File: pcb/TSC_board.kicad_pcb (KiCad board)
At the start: 4 copper layers, 100 x 100 mm, 134 parts, among them IC1 TS3021ILT, IC2 TS3021ILT, IC3 TS3021ILT, IC4 TS3021ILT, IC5 NL17SZ17DFT2G, IC6 NL17SZ17DFT2G, IC7 NL17SZ17DFT2G, IC8 NL17SZ17DFT2G, J1 Conn_01x05_Socket, J2 Conn_01x05_Socket, J3 Conn_01x04_Socket, J4 Conn_01x04_Socket, U1 GAQY212GS, U13 GAQY212GS, U14 GAQY212GS, U15 GAQY212GS, U16 GAQY212GS, U17 GAQY212GS, U18 GAQY212GS, U19 GAQY212GS, U2 DAC7311xDCK, U21 GAQY212GS, U22 GAQY212GS, U23 GAQY212GS, U24 GAQY212GS, U3 LM4040DBZ-5, U4 ADuM1400xRW, U5 ADuM1300xRW, U6 TEA1-0505

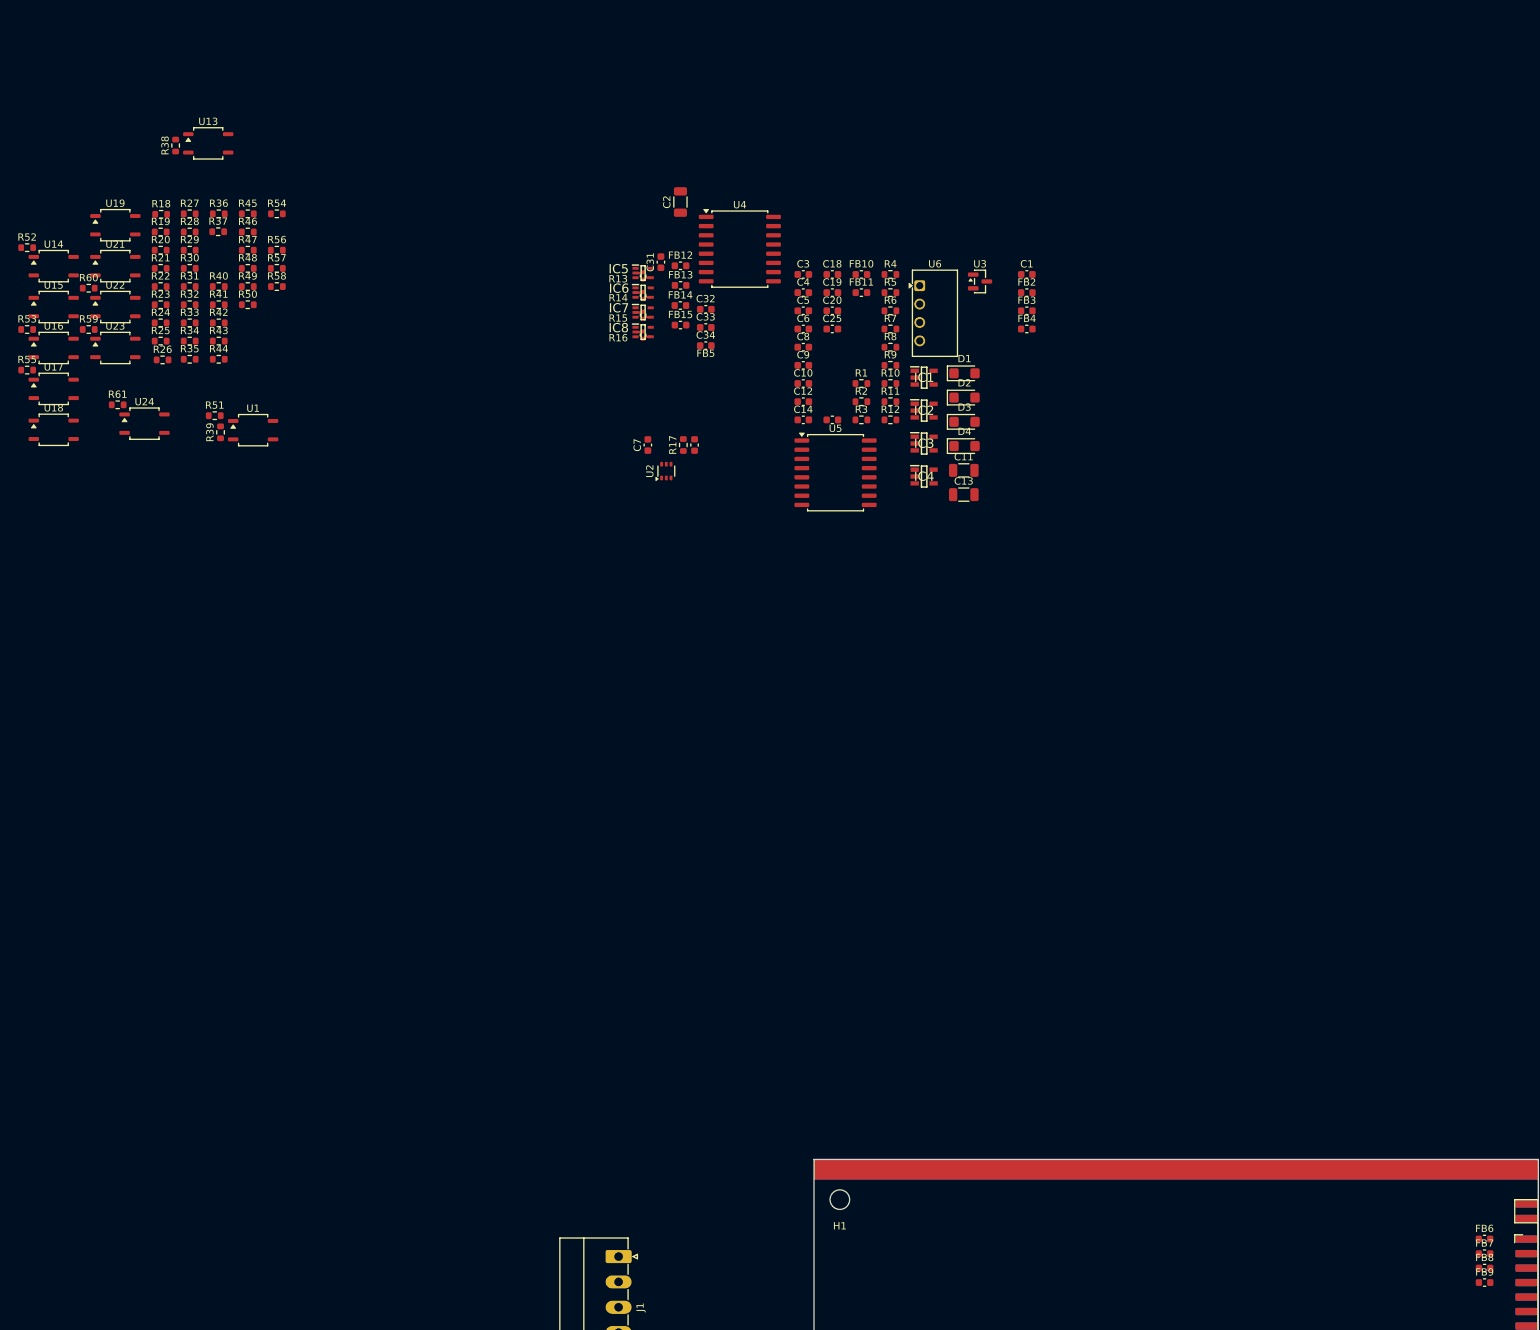
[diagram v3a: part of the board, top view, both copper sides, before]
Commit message: Remove NL17SZ17 symbol; update schematic
Delete the NL17SZ17DFT2G symbol from pcb/Frontend.kicad_sch and apply a bulk update to schematic. Many junction coordinates and UUIDs were regenerated/adjusted in Frontend.kicad_sch; related KiCad files (pcb/MCU.kicad_sch, pcb/TSC_board.kicad_pcb, pcb/TSC_board.kicad_sch) were also updated. This is primarily a cleanup refresh.
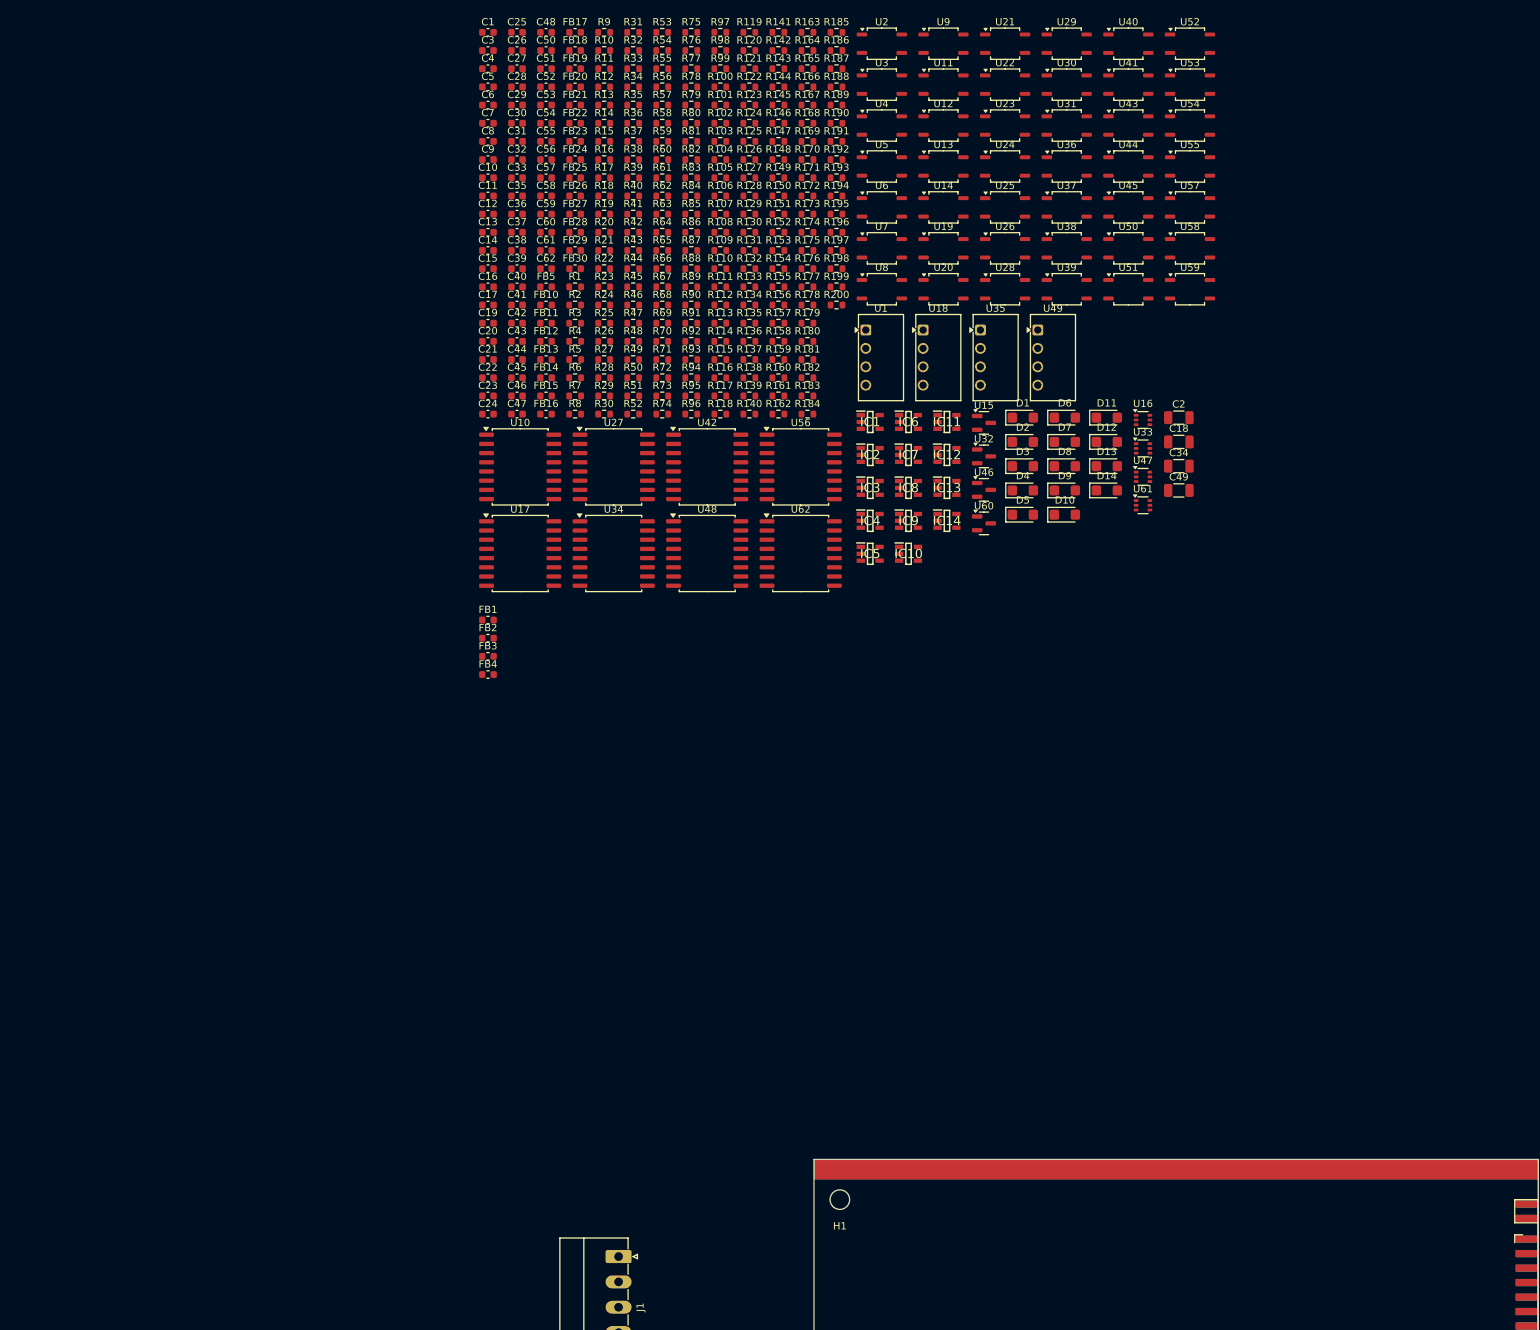
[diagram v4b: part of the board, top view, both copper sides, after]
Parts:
- removed FB6, FB7, FB8, FB9: 100R @ 100MHz, Inductor_SMD:L_0603_1608Metric
- added C15: 100n, Capacitor_SMD:C_0603_1608Metric, F.Cu at (25.0, -73.0)
- added C16: 1n, Capacitor_SMD:C_0603_1608Metric, F.Cu at (25.0, -70.5)
- added C17: 100n, Capacitor_SMD:C_0603_1608Metric, F.Cu at (25.0, -68.0)
- added C21: 100n, Capacitor_SMD:C_0603_1608Metric, F.Cu at (25.0, -60.5)
- added C22: 100n, Capacitor_SMD:C_0603_1608Metric, F.Cu at (25.0, -57.9)
- added C23: 10n, Capacitor_SMD:C_0603_1608Metric, F.Cu at (25.0, -55.4)
- added C24: 100n, Capacitor_SMD:C_0603_1608Metric, F.Cu at (25.0, -52.9)
- added C26: 100n, Capacitor_SMD:C_0603_1608Metric, F.Cu at (29.0, -103.1)
- added C27: 100n, Capacitor_SMD:C_0603_1608Metric, F.Cu at (29.0, -100.6)
- added C28: 100n, Capacitor_SMD:C_0603_1608Metric, F.Cu at (29.0, -98.1)
- added C29: 100n, Capacitor_SMD:C_0603_1608Metric, F.Cu at (29.0, -95.6)
- added C30: 10n, Capacitor_SMD:C_0603_1608Metric, F.Cu at (29.0, -93.1)
- added C35: 10n, Capacitor_SMD:C_0603_1608Metric, F.Cu at (29.0, -83.0)
- added C36: 100n, Capacitor_SMD:C_0603_1608Metric, F.Cu at (29.0, -80.5)
- added C37: 100n, Capacitor_SMD:C_0603_1608Metric, F.Cu at (29.0, -78.0)
- added C38: 100n, Capacitor_SMD:C_0603_1608Metric, F.Cu at (29.0, -75.5)
- added C39: 10n, Capacitor_SMD:C_0603_1608Metric, F.Cu at (29.0, -73.0)
- added C40: 100n, Capacitor_SMD:C_0603_1608Metric, F.Cu at (29.0, -70.5)
- added C41: 100n, Capacitor_SMD:C_0603_1608Metric, F.Cu at (29.0, -68.0)
- added C42: 100n, Capacitor_SMD:C_0603_1608Metric, F.Cu at (29.0, -65.5)
- added C43: 100n, Capacitor_SMD:C_0603_1608Metric, F.Cu at (29.0, -63.0)
- added C44: 100n, Capacitor_SMD:C_0603_1608Metric, F.Cu at (29.0, -60.5)
- added C45: 10n, Capacitor_SMD:C_0603_1608Metric, F.Cu at (29.0, -57.9)
- added C46: 100n, Capacitor_SMD:C_0603_1608Metric, F.Cu at (29.0, -55.4)
- added C47: 1n, Capacitor_SMD:C_0603_1608Metric, F.Cu at (29.0, -52.9)
- added C48: 100n, Capacitor_SMD:C_0603_1608Metric, F.Cu at (33.0, -105.6)
- added C49: 10u, Capacitor_SMD:C_1206_3216Metric, F.Cu at (120.4, -42.4)
- added C50: 10n, Capacitor_SMD:C_0603_1608Metric, F.Cu at (33.0, -103.1)
- added C51: 100n, Capacitor_SMD:C_0603_1608Metric, F.Cu at (33.0, -100.6)
- added C52: 100n, Capacitor_SMD:C_0603_1608Metric, F.Cu at (33.0, -98.1)
- added C53: 100n, Capacitor_SMD:C_0603_1608Metric, F.Cu at (33.0, -95.6)
- added C54: 10n, Capacitor_SMD:C_0603_1608Metric, F.Cu at (33.0, -93.1)
- added C55: 100n, Capacitor_SMD:C_0603_1608Metric, F.Cu at (33.0, -90.6)
- added C56: 100n, Capacitor_SMD:C_0603_1608Metric, F.Cu at (33.0, -88.1)
- added C57: 100n, Capacitor_SMD:C_0603_1608Metric, F.Cu at (33.0, -85.5)
- added C58: 100n, Capacitor_SMD:C_0603_1608Metric, F.Cu at (33.0, -83.0)
- added C59: 100n, Capacitor_SMD:C_0603_1608Metric, F.Cu at (33.0, -80.5)
- added C60: 10n, Capacitor_SMD:C_0603_1608Metric, F.Cu at (33.0, -78.0)
- added C61: 100n, Capacitor_SMD:C_0603_1608Metric, F.Cu at (33.0, -75.5)
- added C62: 1n, Capacitor_SMD:C_0603_1608Metric, F.Cu at (33.0, -73.0)
- added D10: SMF5.0CA, Diode_SMD:D_SMF, F.Cu at (104.7, -39.0)
- added D11: SMF5.0CA, Diode_SMD:D_SMF, F.Cu at (110.5, -52.4)
- added D12: SMF5.0CA, Diode_SMD:D_SMF, F.Cu at (110.5, -49.1)
- added D13: SMF5.0CA, Diode_SMD:D_SMF, F.Cu at (110.5, -45.7)
- added D14: SMF5.0CA, Diode_SMD:D_SMF, F.Cu at (110.5, -42.4)
- added D5: SMF5.0CA, Diode_SMD:D_SMF, F.Cu at (98.9, -39.0)
- added D6: SMF5.0CA, Diode_SMD:D_SMF, F.Cu at (104.7, -52.4)
- added D7: SMF5.0CA, Diode_SMD:D_SMF, F.Cu at (104.7, -49.1)
- added D8: SMF5.0CA, Diode_SMD:D_SMF, F.Cu at (104.7, -45.7)
- added D9: SMF5.0CA, Diode_SMD:D_SMF, F.Cu at (104.7, -42.4)
- added FB16: 100R @ 100MHz, Inductor_SMD:L_0603_1608Metric, F.Cu at (33.0, -52.9)
- added FB17: 100R @ 100MHz, Inductor_SMD:L_0603_1608Metric, F.Cu at (37.1, -105.6)
- added FB18: 100R @ 100MHz, Inductor_SMD:L_0603_1608Metric, F.Cu at (37.1, -103.1)
- added FB19: 100R @ 100MHz, Inductor_SMD:L_0603_1608Metric, F.Cu at (37.1, -100.6)
- added FB20: 100R @ 100MHz, Inductor_SMD:L_0603_1608Metric, F.Cu at (37.1, -98.1)
- added FB21: 100R @ 100MHz, Inductor_SMD:L_0603_1608Metric, F.Cu at (37.1, -95.6)
- added FB22: 100R @ 100MHz, Inductor_SMD:L_0603_1608Metric, F.Cu at (37.1, -93.1)
- added FB23: 100R @ 100MHz, Inductor_SMD:L_0603_1608Metric, F.Cu at (37.1, -90.6)
- added FB24: 100R @ 100MHz, Inductor_SMD:L_0603_1608Metric, F.Cu at (37.1, -88.1)
- added FB25: 100R @ 100MHz, Inductor_SMD:L_0603_1608Metric, F.Cu at (37.1, -85.5)
- added FB26: 100R @ 100MHz, Inductor_SMD:L_0603_1608Metric, F.Cu at (37.1, -83.0)
- added FB27: 100R @ 100MHz, Inductor_SMD:L_0603_1608Metric, F.Cu at (37.1, -80.5)
- added FB28: 100R @ 100MHz, Inductor_SMD:L_0603_1608Metric, F.Cu at (37.1, -78.0)
- added FB29: 100R @ 100MHz, Inductor_SMD:L_0603_1608Metric, F.Cu at (37.1, -75.5)
- added FB30: 100R @ 100MHz, Inductor_SMD:L_0603_1608Metric, F.Cu at (37.1, -73.0)
- added IC10: TS3021ILT, TS3021ILT:SOT95P280X145-5N, F.Cu at (83.1, -33.6)
- added IC11: TS3021ILT, TS3021ILT:SOT95P280X145-5N, F.Cu at (88.4, -51.8)
- added IC12: TS3021ILT, TS3021ILT:SOT95P280X145-5N, F.Cu at (88.4, -47.3)
- added IC13: TS3021ILT, TS3021ILT:SOT95P280X145-5N, F.Cu at (88.4, -42.7)
- added IC14: TS3021ILT, TS3021ILT:SOT95P280X145-5N, F.Cu at (88.4, -38.2)
- added IC9: TS3021ILT, TS3021ILT:SOT95P280X145-5N, F.Cu at (83.1, -38.2)
- added R100: 10k, Resistor_SMD:R_0603_1608Metric, F.Cu at (57.1, -98.1)
- added R101: 10k, Resistor_SMD:R_0603_1608Metric, F.Cu at (57.1, -95.6)
- added R102: 100, Resistor_SMD:R_0603_1608Metric, F.Cu at (57.1, -93.1)
- added R103: 10k, Resistor_SMD:R_0603_1608Metric, F.Cu at (57.1, -90.6)
- added R104: 10k, Resistor_SMD:R_0603_1608Metric, F.Cu at (57.1, -88.1)
- added R105: 10k, Resistor_SMD:R_0603_1608Metric, F.Cu at (57.1, -85.5)
- added R106: 10k, Resistor_SMD:R_0603_1608Metric, F.Cu at (57.1, -83.0)
- added R107: 50k, Resistor_SMD:R_0603_1608Metric, F.Cu at (57.1, -80.5)
- added R108: 1k, Resistor_SMD:R_0603_1608Metric, F.Cu at (57.1, -78.0)
- added R109: 100, Resistor_SMD:R_0603_1608Metric, F.Cu at (57.1, -75.5)
- added R110: 10k, Resistor_SMD:R_0603_1608Metric, F.Cu at (57.1, -73.0)
- added R111: 10k, Resistor_SMD:R_0603_1608Metric, F.Cu at (57.1, -70.5)
- added R112: 10k, Resistor_SMD:R_0603_1608Metric, F.Cu at (57.1, -68.0)
- added R113: 10k, Resistor_SMD:R_0603_1608Metric, F.Cu at (57.1, -65.5)
- added R114: 330R, Resistor_SMD:R_0603_1608Metric, F.Cu at (57.1, -63.0)
- added R115: 50k, Resistor_SMD:R_0603_1608Metric, F.Cu at (57.1, -60.5)
- added R116: 1k, Resistor_SMD:R_0603_1608Metric, F.Cu at (57.1, -57.9)
- added R117: 100, Resistor_SMD:R_0603_1608Metric, F.Cu at (57.1, -55.4)
- added R118: 470, Resistor_SMD:R_0603_1608Metric, F.Cu at (57.1, -52.9)
- added R119: 470, Resistor_SMD:R_0603_1608Metric, F.Cu at (61.1, -105.6)
- added R120: 470, Resistor_SMD:R_0603_1608Metric, F.Cu at (61.1, -103.1)
- added R121: 10k, Resistor_SMD:R_0603_1608Metric, F.Cu at (61.1, -100.6)
- added R122: 10k, Resistor_SMD:R_0603_1608Metric, F.Cu at (61.1, -98.1)
- added R123: 10k, Resistor_SMD:R_0603_1608Metric, F.Cu at (61.1, -95.6)
- added R124: 50k, Resistor_SMD:R_0603_1608Metric, F.Cu at (61.1, -93.1)
- added R125: 10k, Resistor_SMD:R_0603_1608Metric, F.Cu at (61.1, -90.6)
- added R126: 10k, Resistor_SMD:R_0603_1608Metric, F.Cu at (61.1, -88.1)
- added R127: 10k, Resistor_SMD:R_0603_1608Metric, F.Cu at (61.1, -85.5)
- added R128: 1k, Resistor_SMD:R_0603_1608Metric, F.Cu at (61.1, -83.0)
- added R129: 100, Resistor_SMD:R_0603_1608Metric, F.Cu at (61.1, -80.5)
- added R130: 470, Resistor_SMD:R_0603_1608Metric, F.Cu at (61.1, -78.0)
- added R131: 470, Resistor_SMD:R_0603_1608Metric, F.Cu at (61.1, -75.5)
- added R132: 470, Resistor_SMD:R_0603_1608Metric, F.Cu at (61.1, -73.0)
- added R133: 10k, Resistor_SMD:R_0603_1608Metric, F.Cu at (61.1, -70.5)
- added R134: 10k, Resistor_SMD:R_0603_1608Metric, F.Cu at (61.1, -68.0)
- added R135: 10k, Resistor_SMD:R_0603_1608Metric, F.Cu at (61.1, -65.5)
- added R136: 10k, Resistor_SMD:R_0603_1608Metric, F.Cu at (61.1, -63.0)
- added R137: 10k, Resistor_SMD:R_0603_1608Metric, F.Cu at (61.1, -60.5)
- added R138: 10k, Resistor_SMD:R_0603_1608Metric, F.Cu at (61.1, -57.9)
- added R139: 50k, Resistor_SMD:R_0603_1608Metric, F.Cu at (61.1, -55.4)
- added R140: 10k, Resistor_SMD:R_0603_1608Metric, F.Cu at (61.1, -52.9)
- added R141: 10k, Resistor_SMD:R_0603_1608Metric, F.Cu at (65.1, -105.6)
- added R142: 10k, Resistor_SMD:R_0603_1608Metric, F.Cu at (65.1, -103.1)
- added R143: 470, Resistor_SMD:R_0603_1608Metric, F.Cu at (65.1, -100.6)
- added R144: 470, Resistor_SMD:R_0603_1608Metric, F.Cu at (65.1, -98.1)
- added R145: 1k, Resistor_SMD:R_0603_1608Metric, F.Cu at (65.1, -95.6)
- added R146: 470, Resistor_SMD:R_0603_1608Metric, F.Cu at (65.1, -93.1)
- added R147: 10k, Resistor_SMD:R_0603_1608Metric, F.Cu at (65.1, -90.6)
- added R148: 10k, Resistor_SMD:R_0603_1608Metric, F.Cu at (65.1, -88.1)
- added R149: 10k, Resistor_SMD:R_0603_1608Metric, F.Cu at (65.1, -85.5)
- added R150: 100, Resistor_SMD:R_0603_1608Metric, F.Cu at (65.1, -83.0)
- added R151: 10k, Resistor_SMD:R_0603_1608Metric, F.Cu at (65.1, -80.5)
- added R152: 10k, Resistor_SMD:R_0603_1608Metric, F.Cu at (65.1, -78.0)
- added R153: 10k, Resistor_SMD:R_0603_1608Metric, F.Cu at (65.1, -75.5)
- added R154: 10k, Resistor_SMD:R_0603_1608Metric, F.Cu at (65.1, -73.0)
- added R155: 10k, Resistor_SMD:R_0603_1608Metric, F.Cu at (65.1, -70.5)
- added R156: 10k, Resistor_SMD:R_0603_1608Metric, F.Cu at (65.1, -68.0)
- added R157: 330R, Resistor_SMD:R_0603_1608Metric, F.Cu at (65.1, -65.5)
- added R158: 50k, Resistor_SMD:R_0603_1608Metric, F.Cu at (65.1, -63.0)
- added R159: 1k, Resistor_SMD:R_0603_1608Metric, F.Cu at (65.1, -60.5)
- added R160: 100, Resistor_SMD:R_0603_1608Metric, F.Cu at (65.1, -57.9)
- added R161: 470, Resistor_SMD:R_0603_1608Metric, F.Cu at (65.1, -55.4)
- added R162: 470, Resistor_SMD:R_0603_1608Metric, F.Cu at (65.1, -52.9)
- added R163: 470, Resistor_SMD:R_0603_1608Metric, F.Cu at (69.1, -105.6)
- added R164: 10k, Resistor_SMD:R_0603_1608Metric, F.Cu at (69.1, -103.1)
- added R165: 10k, Resistor_SMD:R_0603_1608Metric, F.Cu at (69.1, -100.6)
- added R166: 10k, Resistor_SMD:R_0603_1608Metric, F.Cu at (69.1, -98.1)
- added R167: 50k, Resistor_SMD:R_0603_1608Metric, F.Cu at (69.1, -95.6)
- added R168: 10k, Resistor_SMD:R_0603_1608Metric, F.Cu at (69.1, -93.1)
- added R169: 10k, Resistor_SMD:R_0603_1608Metric, F.Cu at (69.1, -90.6)
- added R170: 10k, Resistor_SMD:R_0603_1608Metric, F.Cu at (69.1, -88.1)
- added R171: 1k, Resistor_SMD:R_0603_1608Metric, F.Cu at (69.1, -85.5)
- added R172: 100, Resistor_SMD:R_0603_1608Metric, F.Cu at (69.1, -83.0)
- added R173: 470, Resistor_SMD:R_0603_1608Metric, F.Cu at (69.1, -80.5)
- added R174: 470, Resistor_SMD:R_0603_1608Metric, F.Cu at (69.1, -78.0)
- added R175: 470, Resistor_SMD:R_0603_1608Metric, F.Cu at (69.1, -75.5)
- added R176: 10k, Resistor_SMD:R_0603_1608Metric, F.Cu at (69.1, -73.0)
- added R177: 10k, Resistor_SMD:R_0603_1608Metric, F.Cu at (69.1, -70.5)
- added R178: 10k, Resistor_SMD:R_0603_1608Metric, F.Cu at (69.1, -68.0)
- added R179: 10k, Resistor_SMD:R_0603_1608Metric, F.Cu at (69.1, -65.5)
- added R180: 10k, Resistor_SMD:R_0603_1608Metric, F.Cu at (69.1, -63.0)
- added R181: 10k, Resistor_SMD:R_0603_1608Metric, F.Cu at (69.1, -60.5)
- added R182: 50k, Resistor_SMD:R_0603_1608Metric, F.Cu at (69.1, -57.9)
- added R183: 10k, Resistor_SMD:R_0603_1608Metric, F.Cu at (69.1, -55.4)
- added R184: 10k, Resistor_SMD:R_0603_1608Metric, F.Cu at (69.1, -52.9)
- added R185: 10k, Resistor_SMD:R_0603_1608Metric, F.Cu at (73.1, -105.6)
- added R186: 470, Resistor_SMD:R_0603_1608Metric, F.Cu at (73.1, -103.1)
- added R187: 470, Resistor_SMD:R_0603_1608Metric, F.Cu at (73.1, -100.6)
- added R188: 1k, Resistor_SMD:R_0603_1608Metric, F.Cu at (73.1, -98.1)
- added R189: 470, Resistor_SMD:R_0603_1608Metric, F.Cu at (73.1, -95.6)
- added R190: 10k, Resistor_SMD:R_0603_1608Metric, F.Cu at (73.1, -93.1)
- added R191: 10k, Resistor_SMD:R_0603_1608Metric, F.Cu at (73.1, -90.6)
- added R192: 10k, Resistor_SMD:R_0603_1608Metric, F.Cu at (73.1, -88.1)
- added R193: 100, Resistor_SMD:R_0603_1608Metric, F.Cu at (73.1, -85.5)
- added R194: 10k, Resistor_SMD:R_0603_1608Metric, F.Cu at (73.1, -83.0)
- added R195: 10k, Resistor_SMD:R_0603_1608Metric, F.Cu at (73.1, -80.5)
- added R196: 10k, Resistor_SMD:R_0603_1608Metric, F.Cu at (73.1, -78.0)
- added R197: 10k, Resistor_SMD:R_0603_1608Metric, F.Cu at (73.1, -75.5)
- added R198: 10k, Resistor_SMD:R_0603_1608Metric, F.Cu at (73.1, -73.0)
- added R199: 10k, Resistor_SMD:R_0603_1608Metric, F.Cu at (73.1, -70.5)
- added R200: 330R, Resistor_SMD:R_0603_1608Metric, F.Cu at (73.1, -68.0)
- added R62: 470, Resistor_SMD:R_0603_1608Metric, F.Cu at (49.1, -83.0)
- added R63: 470, Resistor_SMD:R_0603_1608Metric, F.Cu at (49.1, -80.5)
- added R64: 470, Resistor_SMD:R_0603_1608Metric, F.Cu at (49.1, -78.0)
- added R65: 10k, Resistor_SMD:R_0603_1608Metric, F.Cu at (49.1, -75.5)
- added R66: 10k, Resistor_SMD:R_0603_1608Metric, F.Cu at (49.1, -73.0)
- added R67: 10k, Resistor_SMD:R_0603_1608Metric, F.Cu at (49.1, -70.5)
- added R68: 10k, Resistor_SMD:R_0603_1608Metric, F.Cu at (49.1, -68.0)
- added R69: 50k, Resistor_SMD:R_0603_1608Metric, F.Cu at (49.1, -65.5)
- added R70: 10k, Resistor_SMD:R_0603_1608Metric, F.Cu at (49.1, -63.0)
- added R71: 10k, Resistor_SMD:R_0603_1608Metric, F.Cu at (49.1, -60.5)
- added R72: 10k, Resistor_SMD:R_0603_1608Metric, F.Cu at (49.1, -57.9)
- added R73: 10k, Resistor_SMD:R_0603_1608Metric, F.Cu at (49.1, -55.4)
- added R74: 1k, Resistor_SMD:R_0603_1608Metric, F.Cu at (49.1, -52.9)
- added R75: 100, Resistor_SMD:R_0603_1608Metric, F.Cu at (53.1, -105.6)
- added R76: 470, Resistor_SMD:R_0603_1608Metric, F.Cu at (53.1, -103.1)
- added R77: 470, Resistor_SMD:R_0603_1608Metric, F.Cu at (53.1, -100.6)
- added R78: 470, Resistor_SMD:R_0603_1608Metric, F.Cu at (53.1, -98.1)
- added R79: 470, Resistor_SMD:R_0603_1608Metric, F.Cu at (53.1, -95.6)
- added R80: 10k, Resistor_SMD:R_0603_1608Metric, F.Cu at (53.1, -93.1)
- added R81: 10k, Resistor_SMD:R_0603_1608Metric, F.Cu at (53.1, -90.6)
- added R82: 10k, Resistor_SMD:R_0603_1608Metric, F.Cu at (53.1, -88.1)
- added R83: 10k, Resistor_SMD:R_0603_1608Metric, F.Cu at (53.1, -85.5)
- added R84: 10k, Resistor_SMD:R_0603_1608Metric, F.Cu at (53.1, -83.0)
- added R85: 10k, Resistor_SMD:R_0603_1608Metric, F.Cu at (53.1, -80.5)
- added R86: 10k, Resistor_SMD:R_0603_1608Metric, F.Cu at (53.1, -78.0)
- added R87: 10k, Resistor_SMD:R_0603_1608Metric, F.Cu at (53.1, -75.5)
- added R88: 50k, Resistor_SMD:R_0603_1608Metric, F.Cu at (53.1, -73.0)
- added R89: 10k, Resistor_SMD:R_0603_1608Metric, F.Cu at (53.1, -70.5)
- added R90: 10k, Resistor_SMD:R_0603_1608Metric, F.Cu at (53.1, -68.0)
- added R91: 10k, Resistor_SMD:R_0603_1608Metric, F.Cu at (53.1, -65.5)
- added R92: 10k, Resistor_SMD:R_0603_1608Metric, F.Cu at (53.1, -63.0)
- added R93: 470, Resistor_SMD:R_0603_1608Metric, F.Cu at (53.1, -60.5)
- added R94: 470, Resistor_SMD:R_0603_1608Metric, F.Cu at (53.1, -57.9)
- added R95: 470, Resistor_SMD:R_0603_1608Metric, F.Cu at (53.1, -55.4)
- added R96: 1k, Resistor_SMD:R_0603_1608Metric, F.Cu at (53.1, -52.9)
- added R97: 470, Resistor_SMD:R_0603_1608Metric, F.Cu at (57.1, -105.6)
- added R98: 10k, Resistor_SMD:R_0603_1608Metric, F.Cu at (57.1, -103.1)
- added R99: 10k, Resistor_SMD:R_0603_1608Metric, F.Cu at (57.1, -100.6)
- added U10: ADuM1400xRW, Package_SO:SOIC-16W_7.5x10.3mm_P1.27mm, F.Cu at (29.5, -45.6)
- added U11: GAQY212GS, Package_SO:SOP-4_3.8x4.1mm_P2.54mm, F.Cu at (87.9, -98.4)
- added U12: GAQY212GS, Package_SO:SOP-4_3.8x4.1mm_P2.54mm, F.Cu at (87.9, -92.8)
- added U20: GAQY212GS, Package_SO:SOP-4_3.8x4.1mm_P2.54mm, F.Cu at (87.9, -70.2)
- added U25: GAQY212GS, Package_SO:SOP-4_3.8x4.1mm_P2.54mm, F.Cu at (96.4, -81.5)
- added U26: GAQY212GS, Package_SO:SOP-4_3.8x4.1mm_P2.54mm, F.Cu at (96.4, -75.8)
- added U27: ADuM1400xRW, Package_SO:SOIC-16W_7.5x10.3mm_P1.27mm, F.Cu at (42.4, -45.6)
- added U28: GAQY212GS, Package_SO:SOP-4_3.8x4.1mm_P2.54mm, F.Cu at (96.4, -70.2)
- added U29: GAQY212GS, Package_SO:SOP-4_3.8x4.1mm_P2.54mm, F.Cu at (104.9, -104.1)
- added U30: GAQY212GS, Package_SO:SOP-4_3.8x4.1mm_P2.54mm, F.Cu at (104.9, -98.4)
- added U31: GAQY212GS, Package_SO:SOP-4_3.8x4.1mm_P2.54mm, F.Cu at (104.9, -92.8)
- added U32: LM4040DBZ-5, Package_TO_SOT_SMD:SOT-23, F.Cu at (93.5, -47.1)
- added U33: DAC7311xDCK, Package_TO_SOT_SMD:SOT-363_SC-70-6, F.Cu at (115.5, -48.2)
- added U34: ADuM1300xRW, Package_SO:SOIC-16W_7.5x10.3mm_P1.27mm, F.Cu at (42.4, -33.7)
- added U35: TEA1-0505, Converter_DCDC:Converter_DCDC_TRACO_TEA1-xxxx_THT, F.Cu at (93.0, -64.5)
- added U36: GAQY212GS, Package_SO:SOP-4_3.8x4.1mm_P2.54mm, F.Cu at (104.9, -87.1)
- added U37: GAQY212GS, Package_SO:SOP-4_3.8x4.1mm_P2.54mm, F.Cu at (104.9, -81.5)
- added U38: GAQY212GS, Package_SO:SOP-4_3.8x4.1mm_P2.54mm, F.Cu at (104.9, -75.8)
- added U39: GAQY212GS, Package_SO:SOP-4_3.8x4.1mm_P2.54mm, F.Cu at (104.9, -70.2)
- added U40: GAQY212GS, Package_SO:SOP-4_3.8x4.1mm_P2.54mm, F.Cu at (113.4, -104.1)
- added U41: GAQY212GS, Package_SO:SOP-4_3.8x4.1mm_P2.54mm, F.Cu at (113.4, -98.4)
- added U42: ADuM1300xRW, Package_SO:SOIC-16W_7.5x10.3mm_P1.27mm, F.Cu at (55.3, -45.6)
- added U43: GAQY212GS, Package_SO:SOP-4_3.8x4.1mm_P2.54mm, F.Cu at (113.4, -92.8)
- added U44: GAQY212GS, Package_SO:SOP-4_3.8x4.1mm_P2.54mm, F.Cu at (113.4, -87.1)
- added U45: GAQY212GS, Package_SO:SOP-4_3.8x4.1mm_P2.54mm, F.Cu at (113.4, -81.5)
- added U46: LM4040DBZ-5, Package_TO_SOT_SMD:SOT-23, F.Cu at (93.5, -42.5)
- added U47: DAC7311xDCK, Package_TO_SOT_SMD:SOT-363_SC-70-6, F.Cu at (115.5, -44.3)
- added U48: ADuM1300xRW, Package_SO:SOIC-16W_7.5x10.3mm_P1.27mm, F.Cu at (55.3, -33.7)
- added U49: TEA1-0505, Converter_DCDC:Converter_DCDC_TRACO_TEA1-xxxx_THT, F.Cu at (100.9, -64.5)
- added U50: GAQY212GS, Package_SO:SOP-4_3.8x4.1mm_P2.54mm, F.Cu at (113.4, -75.8)
- added U51: GAQY212GS, Package_SO:SOP-4_3.8x4.1mm_P2.54mm, F.Cu at (113.4, -70.2)
- added U52: GAQY212GS, Package_SO:SOP-4_3.8x4.1mm_P2.54mm, F.Cu at (122.0, -104.1)
- added U53: GAQY212GS, Package_SO:SOP-4_3.8x4.1mm_P2.54mm, F.Cu at (122.0, -98.4)
- added U54: GAQY212GS, Package_SO:SOP-4_3.8x4.1mm_P2.54mm, F.Cu at (122.0, -92.8)
- added U55: GAQY212GS, Package_SO:SOP-4_3.8x4.1mm_P2.54mm, F.Cu at (122.0, -87.1)
- added U56: ADuM1300xRW, Package_SO:SOIC-16W_7.5x10.3mm_P1.27mm, F.Cu at (68.2, -45.6)
- added U57: GAQY212GS, Package_SO:SOP-4_3.8x4.1mm_P2.54mm, F.Cu at (122.0, -81.5)
- added U58: GAQY212GS, Package_SO:SOP-4_3.8x4.1mm_P2.54mm, F.Cu at (122.0, -75.8)
- added U59: GAQY212GS, Package_SO:SOP-4_3.8x4.1mm_P2.54mm, F.Cu at (122.0, -70.2)
- added U60: LM4040DBZ-5, Package_TO_SOT_SMD:SOT-23, F.Cu at (93.5, -37.8)
- added U61: DAC7311xDCK, Package_TO_SOT_SMD:SOT-363_SC-70-6, F.Cu at (115.5, -40.3)
- added U62: ADuM1300xRW, Package_SO:SOIC-16W_7.5x10.3mm_P1.27mm, F.Cu at (68.2, -33.7)
- added U7: GAQY212GS, Package_SO:SOP-4_3.8x4.1mm_P2.54mm, F.Cu at (79.4, -75.8)
- added U8: GAQY212GS, Package_SO:SOP-4_3.8x4.1mm_P2.54mm, F.Cu at (79.4, -70.2)
- added U9: GAQY212GS, Package_SO:SOP-4_3.8x4.1mm_P2.54mm, F.Cu at (87.9, -104.1)
- C11, C13: value 10u -> 100n; footprint Capacitor_SMD:C_1206_3216Metric -> Capacitor_SMD:C_0603_1608Metric
- C18, C34: value 100n -> 10u; footprint Capacitor_SMD:C_0603_1608Metric -> Capacitor_SMD:C_1206_3216Metric
- C19, C3: value 100n -> 10n
- C20: value 10n -> 100n
- C32: value 100n -> 1n
- C7: value 1n -> 10n
- IC5, IC6, IC7, IC8: value NL17SZ17DFT2G -> TS3021ILT; footprint SamacSys_Parts:SOT65P210X110-5N -> TS3021ILT:SOT95P280X145-5N
- R1: value 1k -> 50k
- R10, R11, R9: value 50k -> 10k
- R13, R14, R15, R16: value 0R -> 10k; footprint Resistor_SMD:R_0402_1005Metric -> Resistor_SMD:R_0603_1608Metric
- R17: value 330R -> 1k
- R18, R45: value 10k -> 100
- R19, R20, R21, R22, R36, R37, R38, R40: value 10k -> 470
- R2: value 100 -> 1k
- R3: value 1k -> 100
- R31: value 10k -> 50k
- R39: value 10k -> 1k
- R4, R6: value 100 -> 470
- R5, R7: value 1k -> 470
- R50, R58: value 470 -> 50k
- R51, R59: value 470 -> 1k
- R52, R60: value 470 -> 100
- R53, R54, R55, R56: value 470 -> 10k
- R57: value 470 -> 330R
- R8: value 100 -> 10k
- U1, U18: value GAQY212GS -> TEA1-0505; footprint Package_SO:SOP-4_3.8x4.1mm_P2.54mm -> Converter_DCDC:Converter_DCDC_TRACO_TEA1-xxxx_THT
- U15: value GAQY212GS -> LM4040DBZ-5; footprint Package_SO:SOP-4_3.8x4.1mm_P2.54mm -> Package_TO_SOT_SMD:SOT-23
- U16: value GAQY212GS -> DAC7311xDCK; footprint Package_SO:SOP-4_3.8x4.1mm_P2.54mm -> Package_TO_SOT_SMD:SOT-363_SC-70-6
- U17: value GAQY212GS -> ADuM1300xRW; footprint Package_SO:SOP-4_3.8x4.1mm_P2.54mm -> Package_SO:SOIC-16W_7.5x10.3mm_P1.27mm
- U2: value DAC7311xDCK -> GAQY212GS; footprint Package_TO_SOT_SMD:SOT-363_SC-70-6 -> Package_SO:SOP-4_3.8x4.1mm_P2.54mm
- U3: value LM4040DBZ-5 -> GAQY212GS; footprint Package_TO_SOT_SMD:SOT-23 -> Package_SO:SOP-4_3.8x4.1mm_P2.54mm
- U4: value ADuM1400xRW -> GAQY212GS; footprint Package_SO:SOIC-16W_7.5x10.3mm_P1.27mm -> Package_SO:SOP-4_3.8x4.1mm_P2.54mm
- U5: value ADuM1300xRW -> GAQY212GS; footprint Package_SO:SOIC-16W_7.5x10.3mm_P1.27mm -> Package_SO:SOP-4_3.8x4.1mm_P2.54mm
- U6: value TEA1-0505 -> GAQY212GS; footprint Converter_DCDC:Converter_DCDC_TRACO_TEA1-xxxx_THT -> Package_SO:SOP-4_3.8x4.1mm_P2.54mm
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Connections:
- C1 pad 1: Net-(C1-Pad1) -> Net-(U1--Vout)
- C1 pad 2: Net-(C1-Pad2) -> Net-(U1-+Vout)
- C10 pad 1: Net-(U5-V_{DD2}) -> Net-(IC3-VCC+)
- C10 pad 2: Net-(U5-V_{DD2}) -> Net-(D1-A2)
- C11 pad 1: Net-(U6-+Vout) -> Net-(IC4-VCC+)
- C11 pad 2: Net-(U2-GND) -> Net-(D1-A2)
- C12 pad 1: Net-(U2-GND) -> Net-(U17-V_{DD2})
- C12 pad 2: Net-(U4-VDD1) -> Net-(U17-V_{DD2})
- C13 pad 1: +5V -> Net-(U15-K)
- C13 pad 2: GND -> Net-(U1--Vout)
- C18 pad 1: +5V -> Net-(U18-+Vout)
- C18 pad 2: GND -> Net-(U18--Vout)
- C19 pad 1: +3.3V -> GND
- C19 pad 2: GND -> +5V
- C2 pad 1: Net-(C1-Pad2) -> Net-(U1-+Vout)
- C2 pad 2: Net-(C1-Pad1) -> Net-(U1--Vout)
- C20 pad 1: GND -> +5V
- C20 pad 2: +3.3V -> GND
- C25 pad 1: +3.3V -> Net-(IC6-VCC+)
- C25 pad 2: GND -> Net-(D5-A2)
- C3 pad 1: Net-(IC1-VCC+) -> GND
- C3 pad 2: Net-(D1-A2) -> +5V
- C31 pad 1: Net-(IC5-VCC) -> +3.3V
- C31 pad 2: Net-(IC5-GND) -> GND
- C32 pad 1: Net-(IC6-VCC) -> Net-(U33-VOUT)
- C32 pad 2: Net-(IC5-GND) -> Net-(U18--Vout)
- C33 pad 1: Net-(IC7-VCC) -> Net-(U35--Vout)
- C33 pad 2: Net-(IC5-GND) -> Net-(U35-+Vout)
- C34 pad 1: Net-(IC8-VCC) -> Net-(U35-+Vout)
- C34 pad 2: Net-(IC5-GND) -> Net-(U35--Vout)
- C4 pad 1: Net-(IC2-VCC+) -> +5V
- C4 pad 2: Net-(D1-A2) -> GND
- C5 pad 1: Net-(IC3-VCC+) -> Net-(IC1-VCC+)
- C6 pad 1: Net-(IC4-VCC+) -> Net-(U1--Vout)
- C6 pad 2: Net-(D1-A2) -> Net-(U10-VDD1)
- C7 pad 1: Net-(U2-VOUT) -> GND
- C7 pad 2: Net-(U2-GND) -> +3.3V
- C8 pad 1: Net-(U2-AVDD/AVREF) -> +3.3V
- C8 pad 2: Net-(U2-GND) -> GND
- C9 pad 1: Net-(U2-GND) -> Net-(IC2-VCC+)
- C9 pad 2: Net-(U6-+Vout) -> Net-(D1-A2)
- FB10 pad 1: Net-(U4-VDD1) -> Net-(U17-V_{DD2})
- FB10 pad 2: Net-(U6-+Vout) -> Net-(U1-+Vout)
- FB11 pad 1: Net-(U5-V_{DD2}) -> Net-(FB11-Pad1)
- FB11 pad 2: Net-(U6-+Vout) -> Net-(U1-+Vout)
- FB12 pad 1: Net-(IC5-VCC) -> Net-(IC5-VCC+)
- FB12 pad 2: Net-(U6-+Vout) -> Net-(U18-+Vout)
- FB13 pad 1: Net-(IC6-VCC) -> Net-(U27-VDD1)
- FB13 pad 2: Net-(U6-+Vout) -> Net-(U18-+Vout)
- FB14 pad 1: Net-(IC7-VCC) -> Net-(IC6-VCC+)
- FB14 pad 2: Net-(U6-+Vout) -> Net-(U18-+Vout)
- FB15 pad 1: Net-(IC8-VCC) -> Net-(IC7-VCC+)
- FB15 pad 2: Net-(U6-+Vout) -> Net-(U18-+Vout)
- FB5 pad 2: Net-(U6-+Vout) -> Net-(U1-+Vout)
- IC5 pad 1: unconnected-(IC5-NC-Pad1) -> Net-(IC5-OUT)
- IC5 pad 2: Net-(IC1-OUT) -> Net-(D5-A2)
- IC5 pad 3: Net-(IC5-GND) -> Net-(IC5-IN+)
- IC5 pad 4: Net-(IC5-Y) -> Net-(IC5-IN-)
- IC5 pad 5: Net-(IC5-VCC) -> Net-(IC5-VCC+)
- IC6 pad 1: unconnected-(IC6-NC-Pad1) -> Net-(IC6-OUT)
- IC6 pad 2: Net-(IC2-OUT) -> Net-(D5-A2)
- IC6 pad 3: Net-(IC5-GND) -> Net-(IC6-IN+)
- IC6 pad 4: Net-(IC6-Y) -> Net-(IC6-IN-)
- IC6 pad 5: Net-(IC6-VCC) -> Net-(IC6-VCC+)
- IC7 pad 1: unconnected-(IC7-NC-Pad1) -> Net-(IC7-OUT)
- IC7 pad 2: Net-(IC3-OUT) -> Net-(D5-A2)
- IC7 pad 3: Net-(IC5-GND) -> Net-(IC7-IN+)
- IC7 pad 4: Net-(IC7-Y) -> Net-(IC7-IN-)
- IC7 pad 5: Net-(IC7-VCC) -> Net-(IC7-VCC+)
- IC8 pad 1: unconnected-(IC8-NC-Pad1) -> Net-(IC8-OUT)
- IC8 pad 2: Net-(IC4-OUT) -> Net-(D5-A2)
- IC8 pad 3: Net-(IC5-GND) -> Net-(IC8-IN+)
- IC8 pad 4: Net-(IC8-Y) -> Net-(IC8-IN-)
- IC8 pad 5: Net-(IC8-VCC) -> Net-(IC8-VCC+)
- J2 pad 1: unconnected-(J2-Pin_1-Pad1) -> Net-(J2-Pin_1)
- J2 pad 2: unconnected-(J2-Pin_2-Pad2) -> Net-(J2-Pin_2)
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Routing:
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
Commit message: Update TSC_board schematic and layout
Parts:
- removed FB1, FB4: 100R @ 100MHz, Inductor_SMD:L_0603_1608Metric
- added C63: 100n, Capacitor_SMD:C_0603_1608Metric, B.Cu at (161.0, 116.5)
- added FB31: 100R @ 100MHz, Inductor_SMD:L_0603_1608Metric, B.Cu at (158.8, 114.4)
- added FB6: 100R @ 100MHz, Inductor_SMD:L_0603_1608Metric, F.Cu at (41.6, -60.0)
- added FB7: 100R @ 100MHz, Inductor_SMD:L_0603_1608Metric, F.Cu at (41.6, -57.5)
- added FB8: 100R @ 100MHz, Inductor_SMD:L_0603_1608Metric, F.Cu at (41.6, -55.0)
- added FB9: 100R @ 100MHz, Inductor_SMD:L_0603_1608Metric, F.Cu at (41.6, -52.5)
- added U63: APS6404L-3SQRx-SN, Package_SO:SOIC-8_3.9x4.9mm_P1.27mm, B.Cu at (162.2, 112.0)
- FB2, FB3: moved to B.Cu
- moved U36 262.1 mm to (92.9, 174.7)
- moved U37 262.1 mm to (92.9, 180.3)
- moved U38 262.1 mm to (92.9, 186.0)
- moved U39 262.1 mm to (92.9, 191.7)
- moved U40 262.1 mm to (101.4, 157.8)
- moved U41 262.1 mm to (101.4, 163.4)
- moved U43 262.1 mm to (101.4, 169.1)
- moved U44 262.1 mm to (101.4, 174.7)
- moved U45 262.1 mm to (101.4, 180.3)
- moved FB22 254.3 mm to (135.8, 141.2), turned to 90 degrees
- moved C30 251.6 mm to (162.3, 120.4), turned to -90 degrees
- moved FB21 251.3 mm to (135.9, 135.5), turned to 90 degrees
- moved FB23 250.7 mm to (147.4, 134.5), turned to 90 degrees
- moved FB19 250.7 mm to (135.8, 129.8), turned to 90 degrees
- moved C31 250.3 mm to (163.8, 120.4), turned to 90 degrees
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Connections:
- net /Frontend/CH1_1_IN renamed /Conn/TIM5_CH1
- net /Frontend/CH1_2_IN renamed /Conn/TIM5_CH2
- net /Frontend/CH1_3_IN renamed /Conn/TIM5_CH3
- net /Frontend/CH1_4_IN renamed /Conn/TIM5_CH4
- net /Frontend/CH2_1_IN renamed /Conn/TIM2_CH1
- net /Frontend/CH2_2_IN renamed /Conn/TIM2_CH2
- net /Frontend/CH2_3_IN renamed /Conn/TIM2_CH3
- net /Frontend/CH2_4_IN renamed /Conn/TIM2_CH4
- net /Frontend/CH3_1_IN renamed /Conn/LPTIM1_IN1
- net /Frontend/CH3_2_IN renamed /Conn/LPTIM3_IN1
- net /Frontend/CH3_3_IN renamed /Conn/LPTIM4_IN1
- net /Frontend/CH4_1_IN renamed /Conn/TIM1_ETR
- net /Frontend/CH4_2_IN renamed /Conn/TIM3_ETR
- net /Frontend/CH4_3_IN renamed /Conn/TIM4_ETR
- net /Frontend/DAC_CS1 renamed /Conn/DAC_CS1
- net /Frontend/DAC_CS2 renamed /Conn/DAC_CS2
- net /Frontend/DAC_CS3 renamed /Conn/DAC_CS3
- net /Frontend/DAC_CS4 renamed /Conn/DAC_CS4
- net /Frontend/DAC_MOSI renamed /Conn/DAC_MOSI
- net /Frontend/DAC_SCK renamed /Conn/DAC_SCK
- C1 pad 1: Net-(U1--Vout) -> Net-(D1-A2)
- C13 pad 2: Net-(U1--Vout) -> Net-(D1-A2)
- C16 pad 2: Net-(U1--Vout) -> Net-(D1-A2)
- C17 pad 1: Net-(U18--Vout) -> Net-(D5-A2)
- C18 pad 2: Net-(U18--Vout) -> Net-(D5-A2)
- C2 pad 2: Net-(U1--Vout) -> Net-(D1-A2)
- C22 pad 1: Net-(U18--Vout) -> Net-(D5-A2)
- C29 pad 2: Net-(U18--Vout) -> Net-(D5-A2)
- C32 pad 2: Net-(U18--Vout) -> Net-(D5-A2)
- C33 pad 1: Net-(U35--Vout) -> Net-(D10-A2)
- C34 pad 2: Net-(U35--Vout) -> Net-(D10-A2)
- C38 pad 1: Net-(U35--Vout) -> Net-(D10-A2)
- C43 pad 2: Net-(U48-V_{DD2}) -> Net-(D10-A2)
- C44 pad 2: Net-(U35--Vout) -> Net-(D10-A2)
- C47 pad 2: Net-(U35--Vout) -> Net-(D10-A2)
- C48 pad 1: Net-(U49--Vout) -> Net-(D12-A2)
- C49 pad 2: Net-(U49--Vout) -> Net-(D12-A2)
- C53 pad 1: Net-(U49--Vout) -> Net-(D12-A2)
- C59 pad 2: Net-(U49--Vout) -> Net-(D12-A2)
- C6 pad 1: Net-(U1--Vout) -> Net-(D1-A2)
- C62 pad 2: Net-(U49--Vout) -> Net-(D12-A2)
- J3 pad 4: Net-(J3-Pin_4) -> Net-(D10-A2)
- J4 pad 4: Net-(J4-Pin_4) -> Net-(D12-A2)
- R154 pad 2: Net-(J3-Pin_4) -> Net-(D10-A2)
- R155 pad 2: Net-(J3-Pin_4) -> Net-(D10-A2)
- R156 pad 2: Net-(J3-Pin_4) -> Net-(D10-A2)
- R197 pad 2: Net-(J4-Pin_4) -> Net-(D12-A2)
- R198 pad 2: Net-(J4-Pin_4) -> Net-(D12-A2)
- R199 pad 2: Net-(J4-Pin_4) -> Net-(D12-A2)
- U1 pad 3: Net-(U1--Vout) -> Net-(D1-A2)
- U10 pad 2: Net-(U1--Vout) -> Net-(D1-A2)
- U10 pad 8: Net-(U1--Vout) -> Net-(D1-A2)
- U15 pad 2: Net-(U1--Vout) -> Net-(D1-A2)
- U16 pad 5: Net-(U1--Vout) -> Net-(D1-A2)
- U17 pad 15: Net-(U1--Vout) -> Net-(D1-A2)
- U17 pad 9: Net-(U1--Vout) -> Net-(D1-A2)
- U18 pad 3: Net-(U18--Vout) -> Net-(D5-A2)
- U27 pad 2: Net-(U18--Vout) -> Net-(D5-A2)
- U27 pad 8: Net-(U18--Vout) -> Net-(D5-A2)
- U32 pad 2: Net-(U18--Vout) -> Net-(D5-A2)
- U33 pad 5: Net-(U18--Vout) -> Net-(D5-A2)
- U34 pad 15: Net-(U18--Vout) -> Net-(D5-A2)
- U34 pad 9: Net-(U18--Vout) -> Net-(D5-A2)
- U35 pad 3: Net-(U35--Vout) -> Net-(D10-A2)
- U42 pad 2: Net-(U35--Vout) -> Net-(D10-A2)
- U42 pad 8: Net-(U35--Vout) -> Net-(D10-A2)
- U46 pad 2: Net-(U35--Vout) -> Net-(D10-A2)
- U47 pad 5: Net-(U35--Vout) -> Net-(D10-A2)
- U48 pad 15: Net-(U35--Vout) -> Net-(D10-A2)
- U48 pad 9: Net-(U35--Vout) -> Net-(D10-A2)
- U49 pad 3: Net-(U49--Vout) -> Net-(D12-A2)
- U56 pad 2: Net-(U49--Vout) -> Net-(D12-A2)
- U56 pad 8: Net-(U49--Vout) -> Net-(D12-A2)
- U60 pad 2: Net-(U49--Vout) -> Net-(D12-A2)
- U61 pad 5: Net-(U49--Vout) -> Net-(D12-A2)
- U62 pad 15: Net-(U49--Vout) -> Net-(D12-A2)
- U62 pad 9: Net-(U49--Vout) -> Net-(D12-A2)
- X1 pad 47: /MCU/QSPI_IO3 -> /Conn/QSPI_IO3
- X1 pad 48: /MCU/QSPI_IO2 -> /Conn/QSPI_IO2
- X1 pad 51: /MCU/QSPI_IO1 -> /Conn/QSPI_IO1
- X1 pad 52: /MCU/QSPI_IO0 -> /Conn/QSPI_IO0
- X1 pad 53: /MCU/QSPI_CLK -> /Conn/QSPI_CLK
- X1 pad 58: /MCU/QSPI_NCS -> /Conn/QSPI_NCS
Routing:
- net GND: track 0.00 -> 158.5 mm, vias 0 -> 19
- net +3.3V: track 0.00 -> 145.0 mm, vias 0 -> 9
- net Earth: track 0.00 -> 143.3 mm, vias 0 -> 2
- net /Conn/DAC_SCK: track 0.00 -> 107.4 mm, vias 0 -> 6
- net /Conn/DAC_MOSI: track 0.00 -> 99.7 mm, vias 0 -> 4
- net +5V: track 0.00 -> 88.3 mm
- net /Conn/TIM5_CH4: track 0.00 -> 48.7 mm, vias 0 -> 2
- net /Conn/DAC_CS3: track 0.00 -> 47.5 mm, vias 0 -> 2
- net /Conn/TIM1_ETR: track 0.00 -> 39.5 mm, vias 0 -> 2
- net Net-(U35-+Vout): track 0.00 -> 38.2 mm, vias 0 -> 1
- net /Conn/LPTIM3_IN1: track 0.00 -> 34.7 mm, vias 0 -> 3
- net Net-(U47-VOUT): track 0.00 -> 34.7 mm, vias 0 -> 4
- net /Conn/DAC_CS1: track 0.00 -> 32.7 mm, vias 0 -> 1
- net Net-(IC11-OUT): track 0.00 -> 31.7 mm, vias 0 -> 2
- net /Conn/TIM5_CH3: track 0.00 -> 30.8 mm
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- added copper zone on B.Cu, net GND
- added copper zone on F.Cu, net GND
- added copper zone on In1.Cu, net GND
- added copper zone on B.Cu, net Net-(D10-A2)
- added copper zone on F.Cu, net Net-(D10-A2)
- added copper zone on In1.Cu, net Net-(D10-A2)
- added copper zone on In2.Cu, net Net-(D10-A2)

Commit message: Update TS3021ILT part and more routing
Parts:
- R1, R115, R12, R124, R139, R31, R50: moved to B.Cu
- moved C33 237.0 mm to (142.2, 135.1), turned to 90 degrees
- moved D11 185.4 mm to (122.0, 140.9), turned to -90 degrees
- moved R50 180.7 mm to (131.0, 70.0)
- moved C5 179.5 mm to (133.5, 58.9), turned to 90 degrees
- moved C11 177.7 mm to (133.5, 71.8), turned to 90 degrees
- moved R52 177.2 mm to (127.7, 72.6)
- moved R51 177.1 mm to (127.7, 70.0)
- moved C10 176.2 mm to (133.5, 67.5), turned to 90 degrees
- moved C9 174.7 mm to (133.5, 63.2), turned to 90 degrees
- moved C34 173.9 mm to (139.7, 135.8), turned to -90 degrees
- moved R31 171.7 mm to (131.0, 65.7)
- moved D10 167.5 mm to (122.0, 136.2), turned to -90 degrees
- moved D9 164.1 mm to (122.0, 129.4), turned to 90 degrees
- moved R12 163.3 mm to (131.1, 61.4)
- moved FB9 155.5 mm to (135.0, 71.8), turned to 90 degrees
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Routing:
- net Net-(IC4-OUT): track 0.00 -> 27.7 mm, vias 0 -> 2
- net Net-(IC1-OUT): track 0.00 -> 25.3 mm, vias 0 -> 2
- net Net-(IC3-OUT): track 0.00 -> 24.3 mm, vias 0 -> 2
- net Net-(IC2-OUT): track 0.00 -> 23.3 mm, vias 0 -> 2
- net Net-(D1-A2): track 0.00 -> 14.2 mm, vias 0 -> 7
- net +5V: track 88.3 -> 96.8 mm
- net Net-(D10-A2): track 12.4 -> 19.3 mm, vias 4 -> 6
- net Net-(D10-A1): track 0.00 -> 5.87 mm
- net Net-(D11-A1): track 0.00 -> 5.72 mm
- net Net-(D9-A1): track 0.00 -> 5.70 mm
- net Net-(IC1-VCC+): track 0.00 -> 3.05 mm
- net Net-(IC4-VCC+): track 0.00 -> 3.05 mm
- net Net-(IC3-VCC+): track 0.00 -> 3.05 mm
- net Net-(IC2-VCC+): track 0.00 -> 3.05 mm
- net Net-(IC9-OUT): track 23.8 -> 26.7 mm
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- added copper zone on B.Cu, net Net-(D1-A2)
- added copper zone on F.Cu, net Net-(D1-A2)
- added copper zone on In1.Cu, net Net-(D1-A2)
- added copper zone on In2.Cu, net Net-(D1-A2)
